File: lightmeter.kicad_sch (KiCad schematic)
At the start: 39 parts, among them J1 5V input, J2 programmer, J3 USB_C_Receptacle_USB2.0_16P, J4 VEML7700, J5 BoostConverterInput, J6 Conn_01x04_Socket, SW1 Shutter, SW2 Value Rot, SW3 BOOT, SW4 Setting Rot, U1 NCP1117-3.3_SOT223, U2 ESP32-S3-WROOM-1

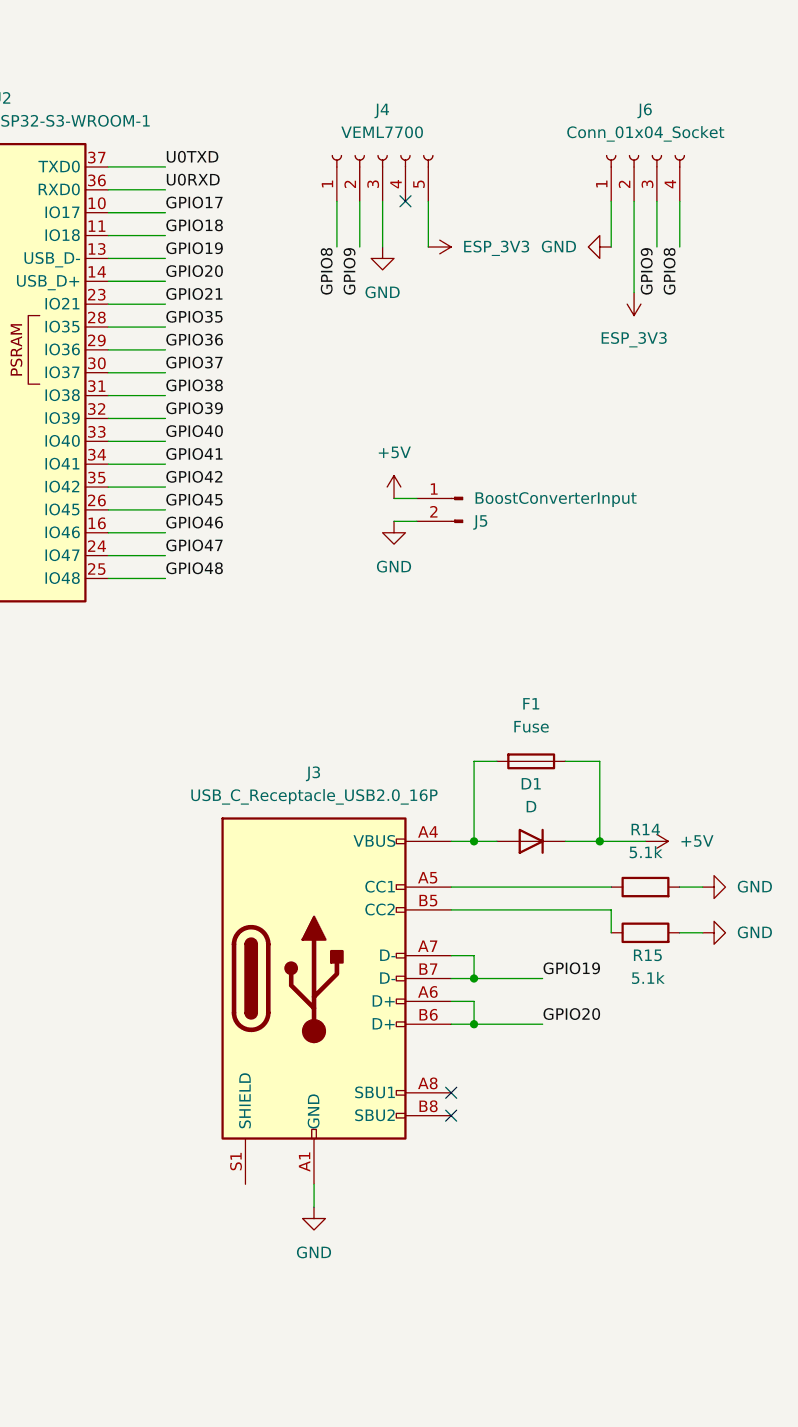
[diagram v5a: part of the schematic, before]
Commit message: Assigned footprints to all components
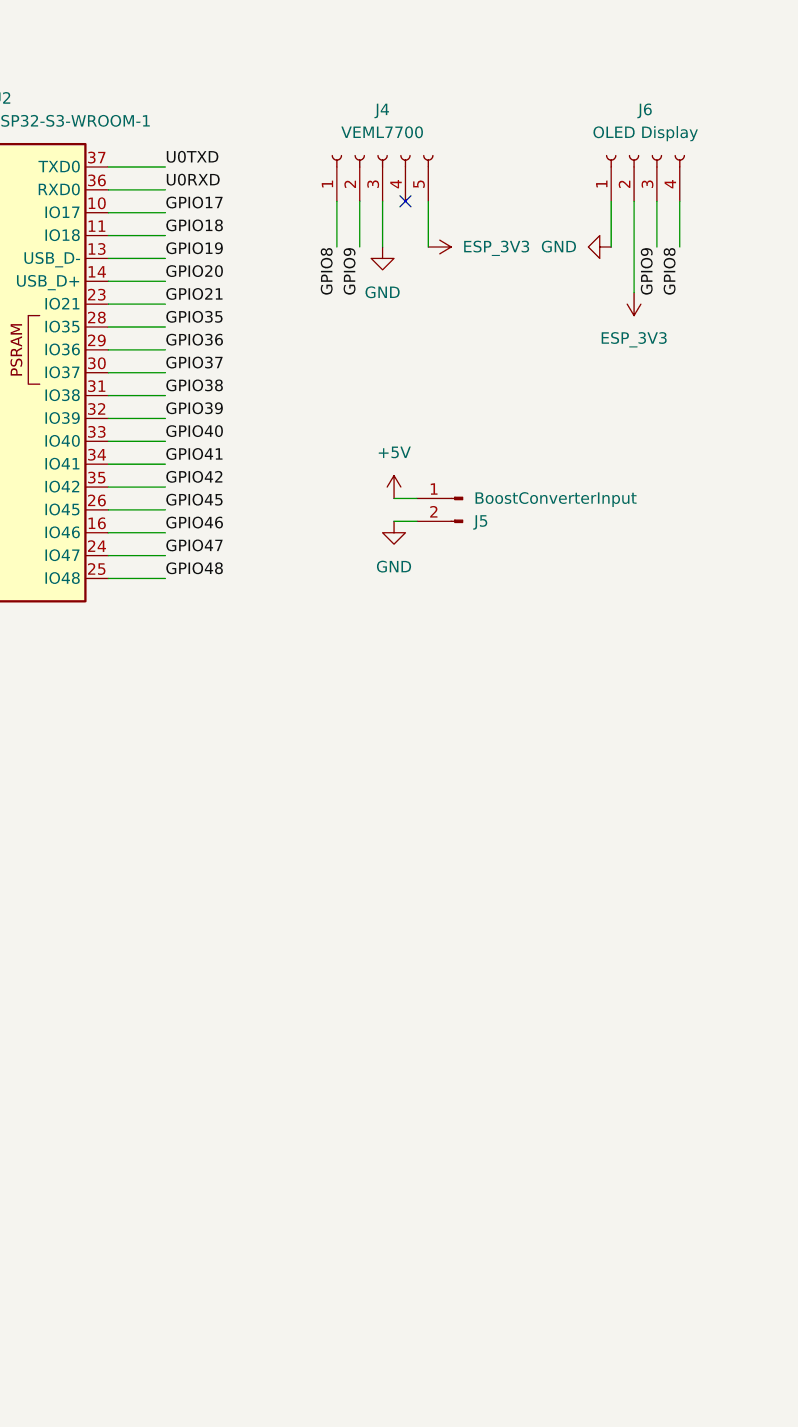
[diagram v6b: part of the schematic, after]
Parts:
- removed D1: D, symbol Device:D
- removed F1: Fuse, symbol Device:Fuse
- removed J3: USB_C_Receptacle_USB2.0_16P, symbol Connector:USB_C_Receptacle_USB2.0_16P
- removed R14, R15: 5.1k, symbol Device:R
- C1, C2, C3, C4, C5, C8, C9: footprint (none) -> Capacitor_SMD:C_0805_2012Metric
- C10: footprint Capacitor_SMD:C_0603_1608Metric_Pad1.08x0.95mm_HandSolder -> Capacitor_SMD:C_0805_2012Metric
- C6: footprint Capacitor_SMD:C_1210_3225Metric -> Capacitor_SMD:C_0805_2012Metric
- C7: footprint Capacitor_SMD:C_0603_1608Metric -> Capacitor_SMD:C_0805_2012Metric
- J1, J5: footprint (none) -> Connector_JST:JST_EH_B2B-EH-A_1x02_P2.50mm_Vertical
- J2, J4: footprint (none) -> Connector_JST:JST_EH_B5B-EH-A_1x05_P2.50mm_Vertical
- J6: value Conn_01x04_Socket -> OLED Display; footprint (none) -> Connector_JST:JST_EH_B4B-EH-A_1x04_P2.50mm_Vertical
- R1, R11, R12, R13, R2, R3, R4, R5, R6, R8, R9: footprint (none) -> Resistor_SMD:R_0805_2012Metric
- R10: footprint Fuse:Fuse_0805_2012Metric -> Fuse:Fuse_1206_3216Metric
- R7: footprint Resistor_SMD:R_0612_1632Metric -> Resistor_SMD:R_0805_2012Metric
- SW1, SW3: footprint (none) -> Button_Switch_THT:SW_PUSH-12mm
- SW2, SW4: footprint (none) -> Rotary_JST:Rotary_JST
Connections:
- no-connect marks 3 -> 1

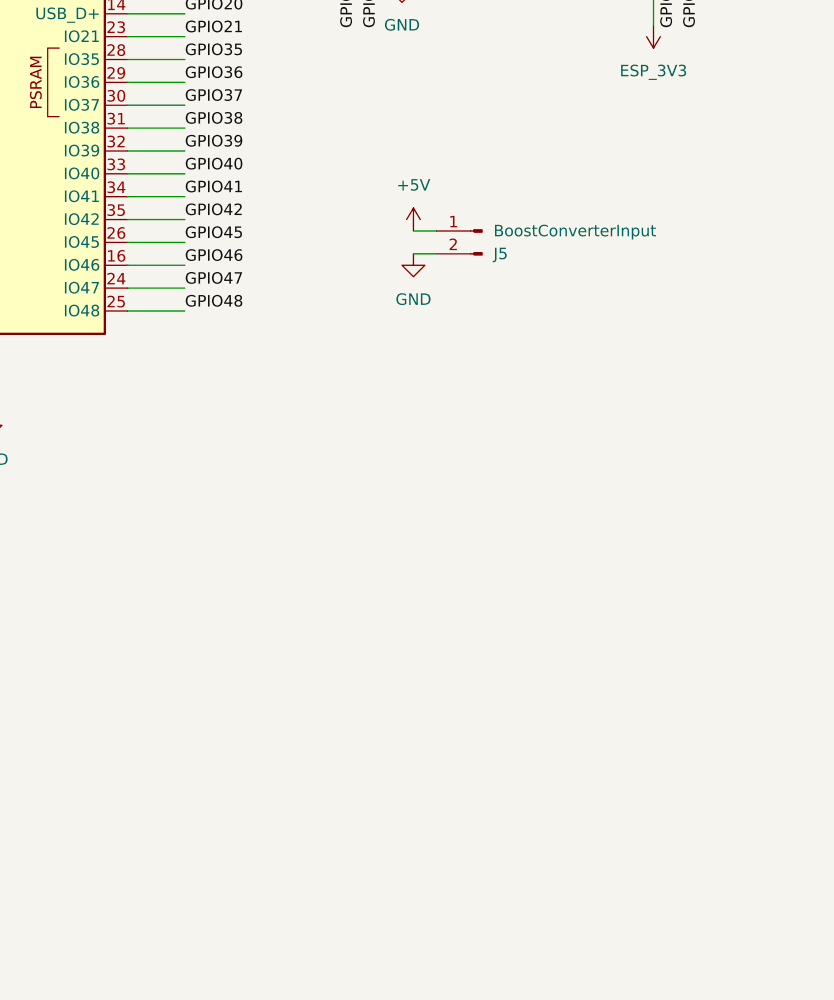
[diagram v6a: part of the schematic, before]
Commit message: Fixed the solanoid control part of the schematic as well as the connector for the VEML7700 light sensor, now I am really ready to start the layout proccess
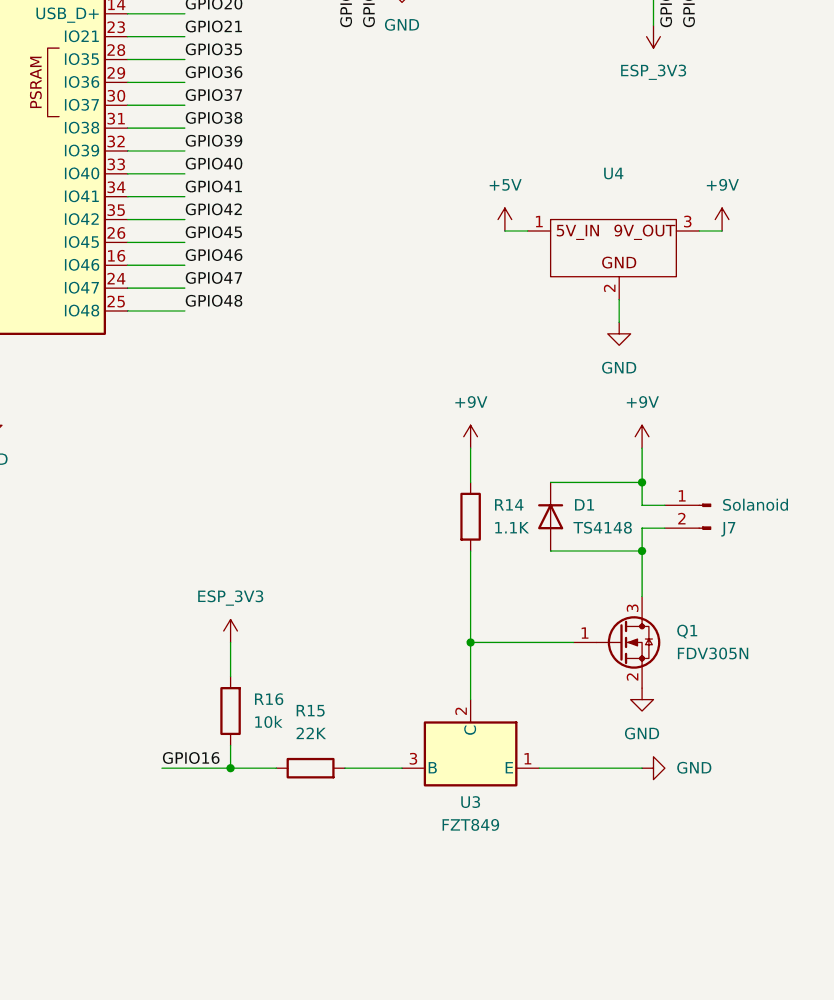
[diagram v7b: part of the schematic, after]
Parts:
- removed J5: BoostConverterInput, Connector_JST:JST_EH_B2B-EH-A_1x02_P2.50mm_Vertical, symbol Connector:Conn_01x02_Pin
- added D1: TS4148, Diode_SMD:D_0805_2012Metric, symbol Device:D
- added J7: Solanoid, Connector_JST:JST_EH_B2B-EH-A_1x02_P2.50mm_Vertical, symbol Connector:Conn_01x02_Pin
- added Q1: FDV305N, Package_TO_SOT_SMD:SOT-23, symbol Transistor_FET:BSS123
- added R14: 1.1K, Resistor_SMD:R_0805_2012Metric, symbol Device:R
- added R15: 22K, Resistor_SMD:R_0805_2012Metric, symbol Device:R
- added R16: 10k, Resistor_SMD:R_0805_2012Metric, symbol Device:R
- added U3: FZT849, Package_TO_SOT_SMD:SOT-223-3_TabPin2, symbol Regulator_Linear:LT1129-3.3_SOT223
- added U4: ~, Boost_Converter_Module_Footprint:Boost_Converter_Module, symbol boost_converter_module:boost_converter_module
- J4: footprint Connector_JST:JST_EH_B5B-EH-A_1x05_P2.50mm_Vertical -> Connector_PinHeader_2.54mm:PinHeader_1x05_P2.54mm_Vertical
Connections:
- net +5V: now also U4.1
- net ESP_3V3: now also R16.2
- net GND: now also Q1.2 (S), U3.1 (E), U4.2
- net GPIO16: now also R15.1, R16.1
- new net: Q1.1 (G), R14.2, U3.2 (C)
- new net: R15.2, U3.3 (B)
- new net: D1.2 (A), J7.2 (Pin_2), Q1.3 (D)
- new net +9V: D1.1 (K), J7.1 (Pin_1), R14.1, U4.3

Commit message: Fixed a few wrong footprints
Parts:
- SW1: footprint Button_Switch_THT:SW_PUSH-12mm -> Vertical_Push_Button:Vertical_Push_Button
- SW3: footprint Button_Switch_THT:SW_PUSH-12mm -> Button_Switch_THT:SW_PUSH_1P1T_6x3.5mm_H4.3_APEM_MJTP1243
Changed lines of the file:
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@@
 			)
 		)
-		(property "Footprint" "Button_Switch_THT:SW_PUSH-12mm"
+		(property "Footprint" "Vertical_Push_Button:Vertical_Push_Button"
 			(at 46.99 125.73 0)
 			(effects
@@
 			)
 		)
-		(property "Footprint" "Button_Switch_THT:SW_PUSH-12mm"
+		(property "Footprint" "Button_Switch_THT:SW_PUSH_1P1T_6x3.5mm_H4.3_APEM_MJTP1243"
 			(at 88.9 111.76 0)
 			(effects
